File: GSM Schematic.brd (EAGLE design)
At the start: 100 x 80 mm, 19 parts, among them J1 5.5x2.1mm Barrel, Q2 16M, U2 LM317MDT-TR

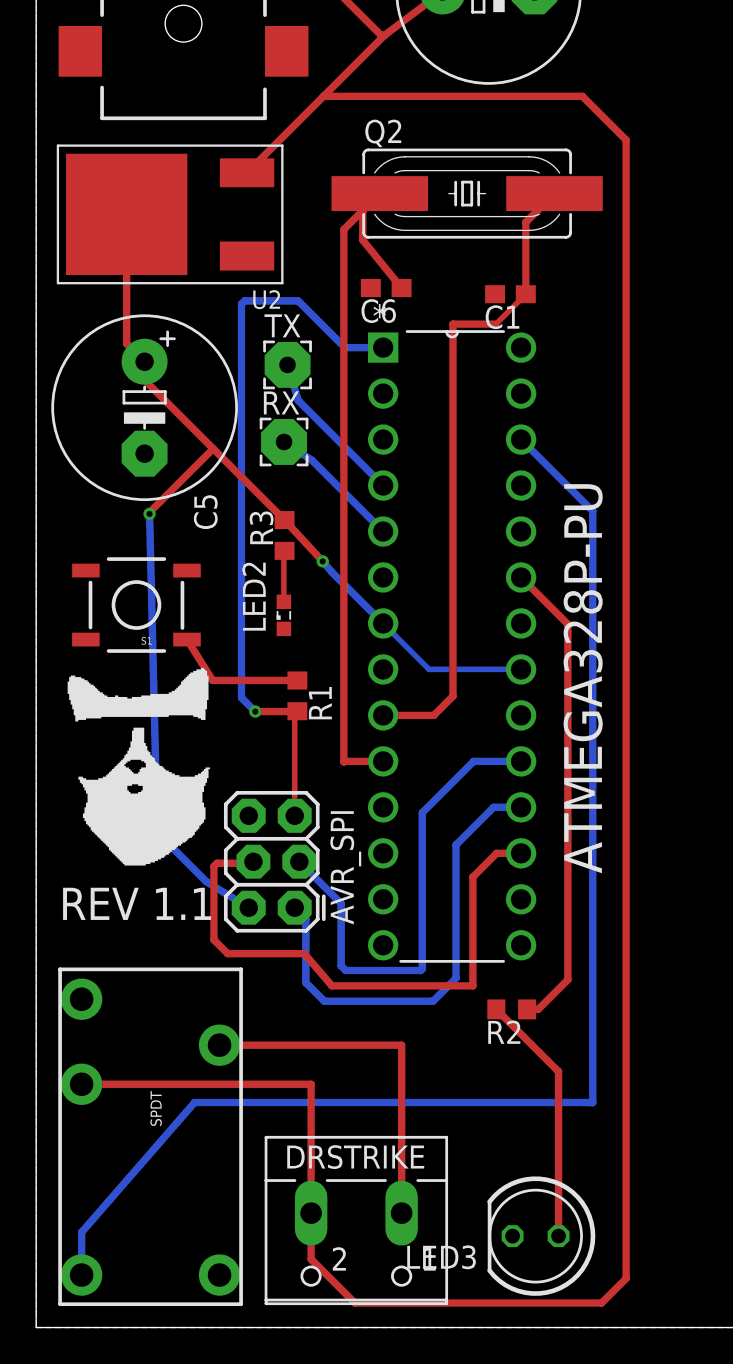
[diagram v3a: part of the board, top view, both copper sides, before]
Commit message: Fixed DRC errors - Down to 10 errors
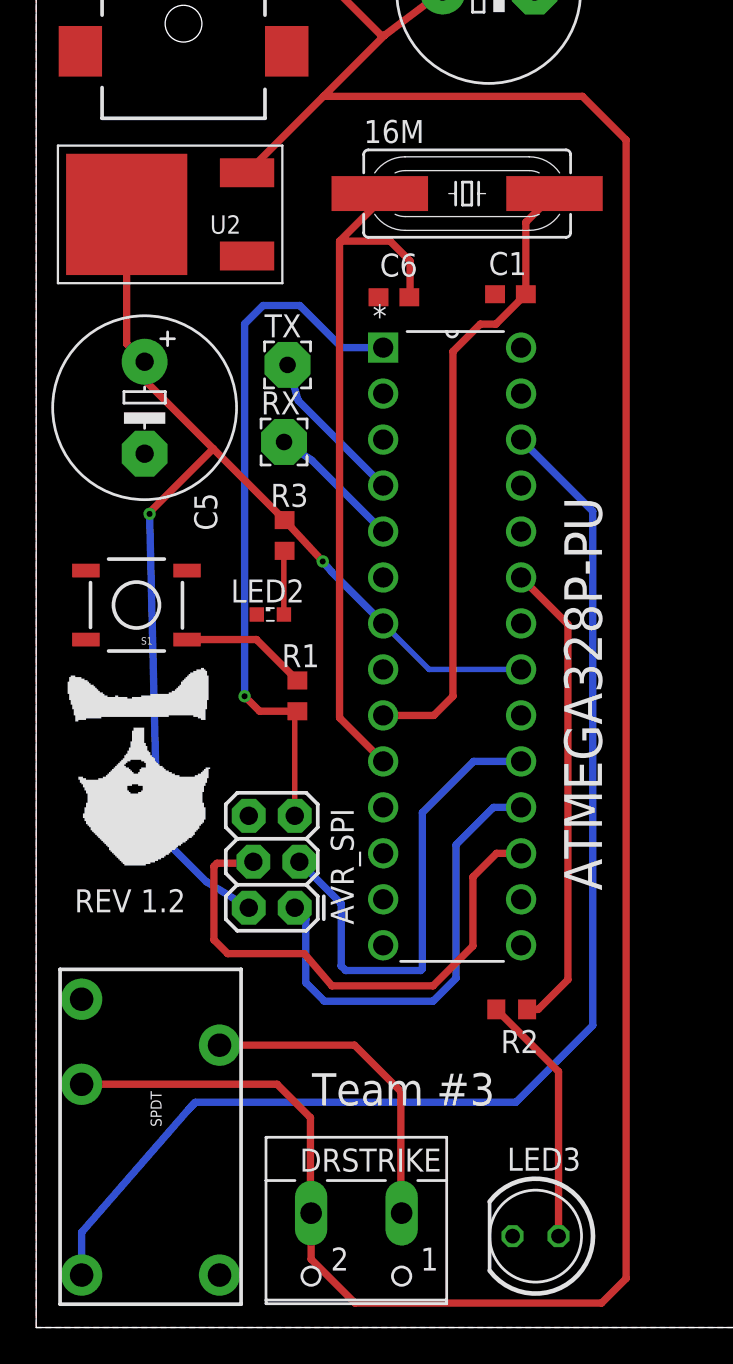
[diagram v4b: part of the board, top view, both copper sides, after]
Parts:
- 16M: value 16M -> (none)
- C1, C6: value 22p -> (none)
- R1: value 10k -> (none)
- R2, R3: value 220 -> (none)
- S1: value TAC_SWITCHSMD -> (none)
- moved LED2 0.75 mm to (12.9, 39.4), turned to 0 degrees
- moved C6 0.66 mm to (19.8, 56.9)
- renumbered Q2 to 16M
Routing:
- net N$14: track 72.1 -> 70.1 mm
- net N$4: track 19.3 -> 17.8 mm
- net N$7: track 31.0 -> 29.7 mm
- net N$10: track 40.0 -> 38.7 mm
- net N$16: track 35.8 -> 34.9 mm
- net N$3: track 2.83 -> 3.53 mm
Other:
- board text added: "REV 1.2"
- board text added: "Team #3"
- board text removed: "REV 1.1"

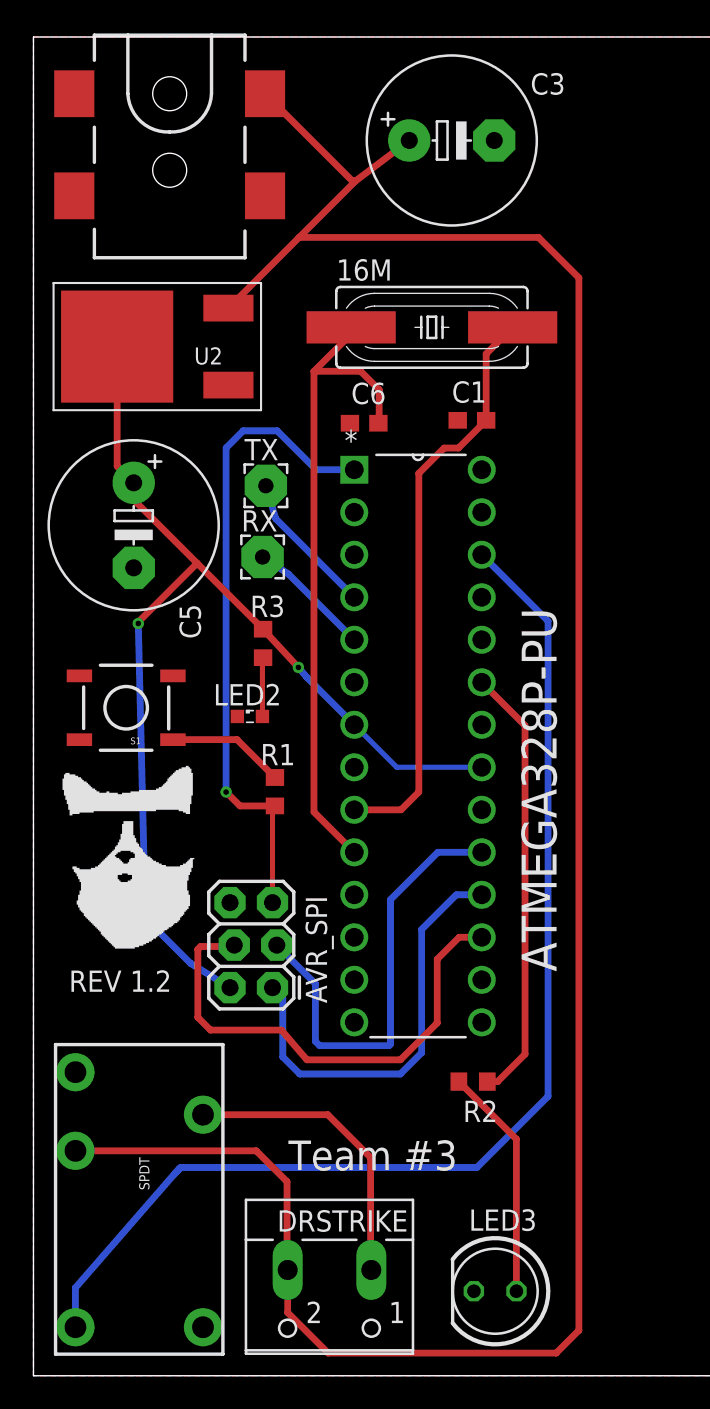
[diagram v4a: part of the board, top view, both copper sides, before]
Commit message: Add files via upload
Added diode to door strike output and cleaned up breadboard lines.
Also solved consistency errors
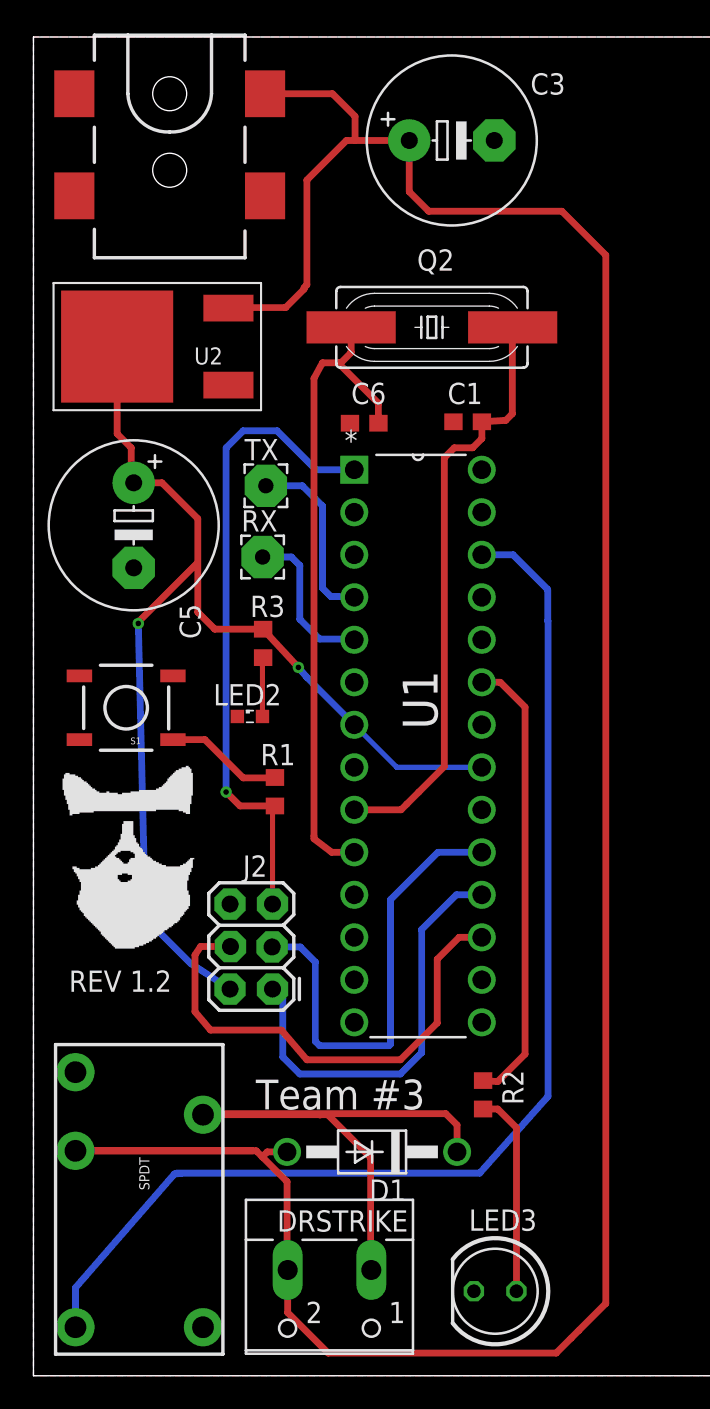
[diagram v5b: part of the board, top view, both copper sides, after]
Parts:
- removed AVR_SPI: (no value), SparkFun-Connectors:2X3_LOCK
- added D1: (no value), diode:DO41-10
- added J2: (no value), SparkFun-Connectors:2X3_LOCK
- moved R2 0.99 mm to (26.9, 16.8), turned to 270 degrees
- moved C1 0.27 mm to (25.9, 57.0)
- renumbered 16M to Q2, ATMEGA328P-PU to U1
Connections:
- new net S$2: J2.2
- net 12V: now also D1.A
- net 5V: no longer AVR_SPI.2
- net GND: now also J2.6; no longer AVR_SPI.6
- net N$10: now also J2.5; no longer AVR_SPI.5
- net N$4: now also D1.C
- net N$5: now also J2.3; no longer AVR_SPI.3
- net N$7: now also J2.4; no longer AVR_SPI.4
- net N$8: now also J2.1; no longer AVR_SPI.1
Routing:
- net S$2: track 0.00 -> 29.3 mm, vias 0 -> 1
- net 5V: track 66.3 -> 39.7 mm, vias 2 -> 1
- net N$4: track 17.8 -> 34.9 mm
- net 12V: track 143.8 -> 160.5 mm
- net N$1: track 8.69 -> 10.9 mm
- net N$12: track 7.41 -> 9.41 mm
- net N$6: track 14.0 -> 12.2 mm
- net N$14: track 70.1 -> 71.3 mm
- net N$5: track 26.6 -> 27.6 mm
- net N$9: track 26.2 -> 27.1 mm
- net N$16: track 34.9 -> 35.8 mm

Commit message: Made board and schematic consistent - no ERC erros
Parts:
- C1, C6: value (none) -> 22p
- D1: value (none) -> 1N4004
- J2: value (none) -> AVR_SPI_PRG_62X3_LOCK
- Q2: value (none) -> 16M
- R1: value (none) -> 10k
- R2, R3: value (none) -> 220
- S1: value (none) -> TAC_SWITCHSMD
- U1: value (none) -> ATMEGA328P-PU
- moved J2 1.05 mm to (15.3, 22.9)
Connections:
- removed net S$2: J2.2
- net 5V: now also J2.2
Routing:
- net 5V: track 39.7 -> 69.1 mm
- net S$2: track 29.3 -> 0.00 mm, vias 1 -> 0
- net N$7: track 29.5 -> 33.7 mm
- net N$8: track 25.4 -> 29.3 mm
- net N$5: track 27.6 -> 28.6 mm

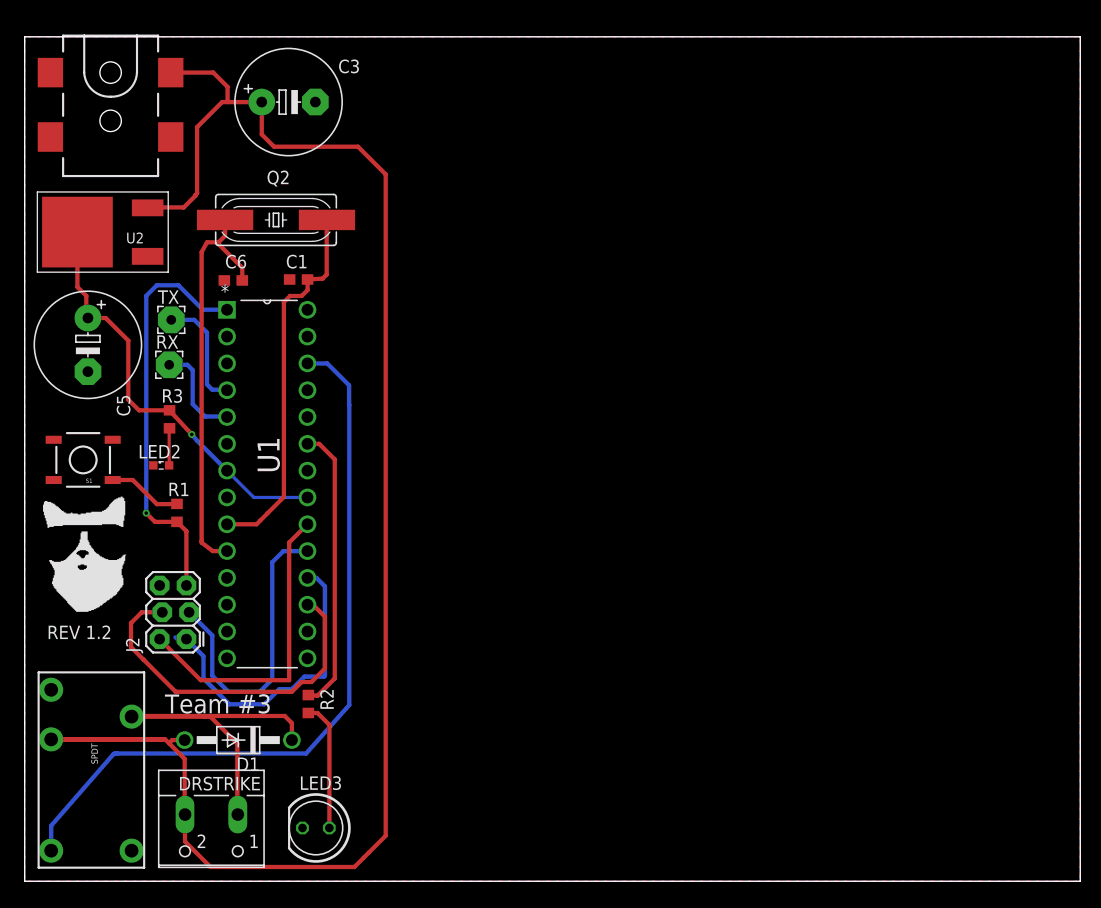
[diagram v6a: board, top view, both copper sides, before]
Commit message: Fixed some DRC errors
Down to 10 errors again
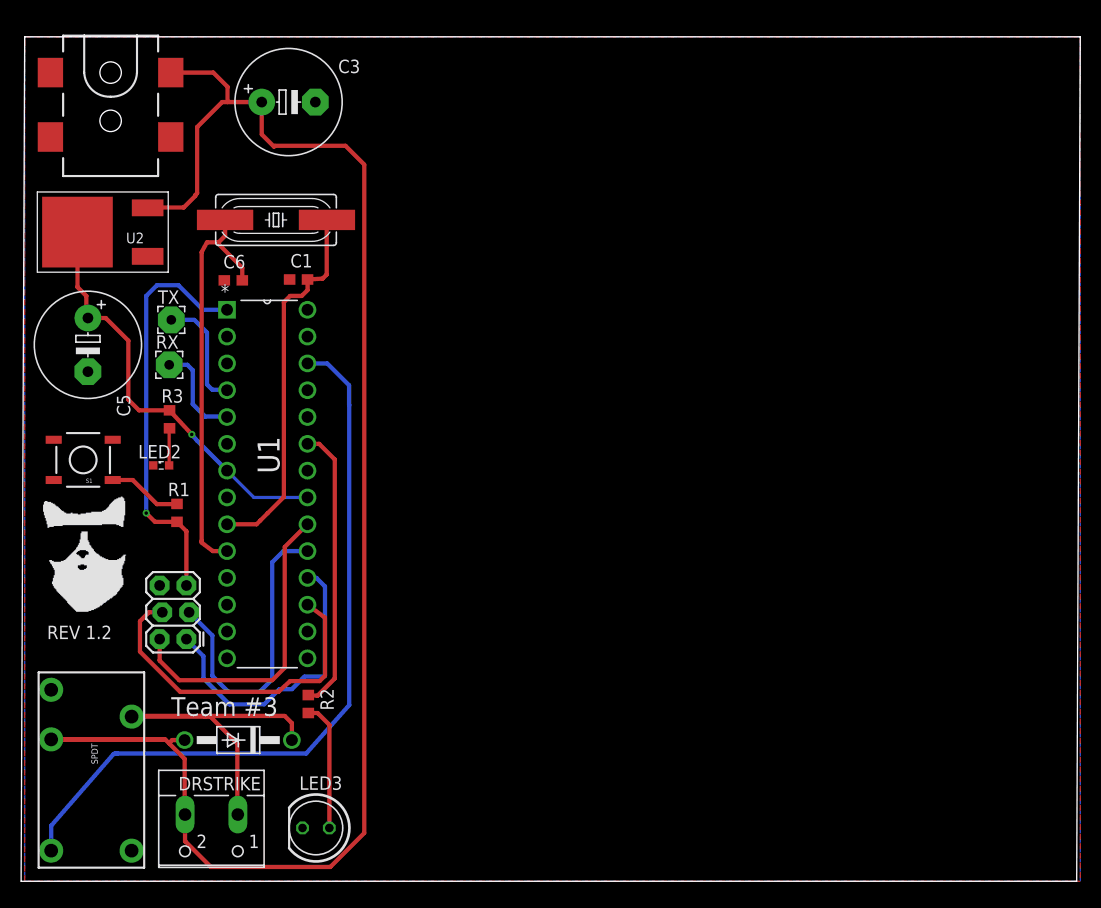
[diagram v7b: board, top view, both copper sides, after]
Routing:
- net 12V: track 160.5 -> 156.9 mm
- net N$7: track 33.7 -> 32.6 mm
- net N$8: track 29.3 -> 28.5 mm
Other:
- board size 100 x 80 mm -> 100.3 x 80 mm

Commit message: timed and added mounting holes
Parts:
- moved LED3 2.88 mm to (27.7, 7.93)
- moved C5 2.21 mm to (6.16, 48.6)
- moved C3 1.52 mm to (23.5, 73.8)
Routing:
- net 12V: track 156.9 -> 150.9 mm
- net N$6: track 12.2 -> 8.87 mm
- net 5V: track 69.4 -> 67.3 mm
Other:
- board size 100.3 x 80 mm -> 33.8 x 80.3 mm
